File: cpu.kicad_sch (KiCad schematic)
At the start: 33 parts, among them IC12 DS2401+, IC13 ARM250, IC20 74HC138, IC27 74AC32, IC8 74HCT14, X4 72.0MHz, X5 25.175MHz

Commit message: yet more traces
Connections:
- net at C84.1, IC13.7 (~{Por}), R94.2: now also D19.1 (A); no longer D19.2 (A)
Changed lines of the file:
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@@
 		(lib_id "Device:D_Dual_CommonCathode_AAK")
 		(at 106.68 62.23 90)
-		(mirror x)
 		(unit 1)
 		(exclude_from_sim no)

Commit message: keyboard routing
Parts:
- added R83, R84, R85, R86, R87, R88, R91: 4K7, Resistor_SMD:R_0805_2012Metric, symbol Device:R_Small
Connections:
- net +5V: now also R83.2, R84.2, R85.2, R86.2, R87.2, R88.2, R91.1
- net ~{Fintr}: now also R85.1
- net ~{Pfiq}: now also R84.1
- net ~{Pirq}: now also R83.1
- net ~{Sintr}: now also R86.1
- net ~{EFiq}: now reaches IC13.134 (Efiq)
- net ~{EFiq}: now also R87.1
- net at IC13.138 (C2): now also R88.1
- net at IC13.143 (~{I13}): now also R91.2
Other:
- moved on the sheet: R218

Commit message: more analogue video work
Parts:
- added CX1: 47pF, Capacitor_THT:C_Axial_L5.1mm_D3.1mm_P12.50mm_Horizontal, symbol Device:C_Small
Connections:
- net ~{Rst}: now also CX1.2
- net at C98.2, C99.2: now also CX1.1
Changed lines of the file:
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@@
 	)
 	(junction
+		(at 71.12 88.9)
+		(diameter 0)
+		(color 0 0 0 0)
+	)
+	(junction
 		(at 187.96 86.36)
 		(diameter 0)
@@
 	(wire
 		(pts
-			(xy 63.5 88.9) (xy 78.74 88.9)
+			(xy 63.5 88.9) (xy 71.12 88.9)
 		)
 		(stroke
@@
 	(wire
 		(pts
+			(xy 71.12 88.9) (xy 71.12 90.17)
+		)
+		(stroke
+			(width 0)
+			(type default)
+		)
+	)
+	(wire
+		(pts
 			(xy 68.58 137.16) (xy 73.66 137.16)
 		)
@@
 		)
 	)
+	(wire
+		(pts
+			(xy 71.12 96.52) (xy 71.12 95.25)
+		)
+		(stroke
+			(width 0)
+			(type default)
+		)
+	)
 	(bus
 		(pts
@@
 	(wire
 		(pts
+			(xy 71.12 88.9) (xy 78.74 88.9)
+		)
+		(stroke
+			(width 0)
+			(type default)
+		)
+	)
+	(wire
+		(pts
 			(xy 186.69 232.41) (xy 189.23 232.41)
 		)
@@
 		)
 	)
+	(global_label "~{Rst}"
+		(shape input)
+		(at 71.12 96.52 0)
+		(fields_autoplaced yes)
+		(effects
+			(font
+				(size 1.27 1.27)
+			)
+			(justify left)
+		)
+		(property "Intersheetrefs" "${INTERSHEET_REFS}"
+			(at 77.129 96.52 0)
+			(effects
+				(font
+					(size 1.27 1.27)
+				)
+				(justify left)
+				(hide yes)
+			)
+		)
+	)
 	(global_label "SndVSS"
 		(shape passive)
@@
 				)
 			)
+		)
+	)
+	(symbol
+		(lib_id "Device:C_Small")
+		(at 71.12 92.71 0)
+		(mirror y)
+		(unit 1)
+		(exclude_from_sim no)
+		(in_bom yes)
+		(on_board yes)
+		(dnp no)
+		(property "Reference" "CX1"
+			(at 73.66 93.9865 0)
+			(effects
+				(font
+					(size 1.27 1.27)
+				)
+				(justify right)
+			)
+		)
+		(property "Value" "47pF"
+			(at 73.66 91.4465 0)
+			(effects
+				(font
+					(size 1.27 1.27)
+				)
+				(justify right)
+			)
+		)
+		(property "Footprint" "Capacitor_THT:C_Axial_L5.1mm_D3.1mm_P12.50mm_Horizontal"
+			(at 71.12 92.71 0)
+			(effects
+				(font
+					(size 1.27 1.27)
+				)
+				(hide yes)
+			)
+		)
+		(property "Datasheet" "~"
+			(at 71.12 92.71 0)
+			(effects
+				(font
+					(size 1.27 1.27)
+				)
+				(hide yes)
+			)
+		)
+		(property "Description" "Unpolarized capacitor, small symbol"
+			(at 71.12 92.71 0)
+			(effects
+				(font
+					(size 1.27 1.27)
+				)
+				(hide yes)
+			)
+		)
+		(pin "1"
+		)
+		(pin "2"
+		)
+		(instances
+			(project "Acorn-A3010"
+				(path "/999882f3-94f8-4a89-9093-27a47d0cb289/5f74aac3-9761-4bed-8486-119acb837e61"
+					(reference "CX1")
+					(unit 1)
+				)
+			)

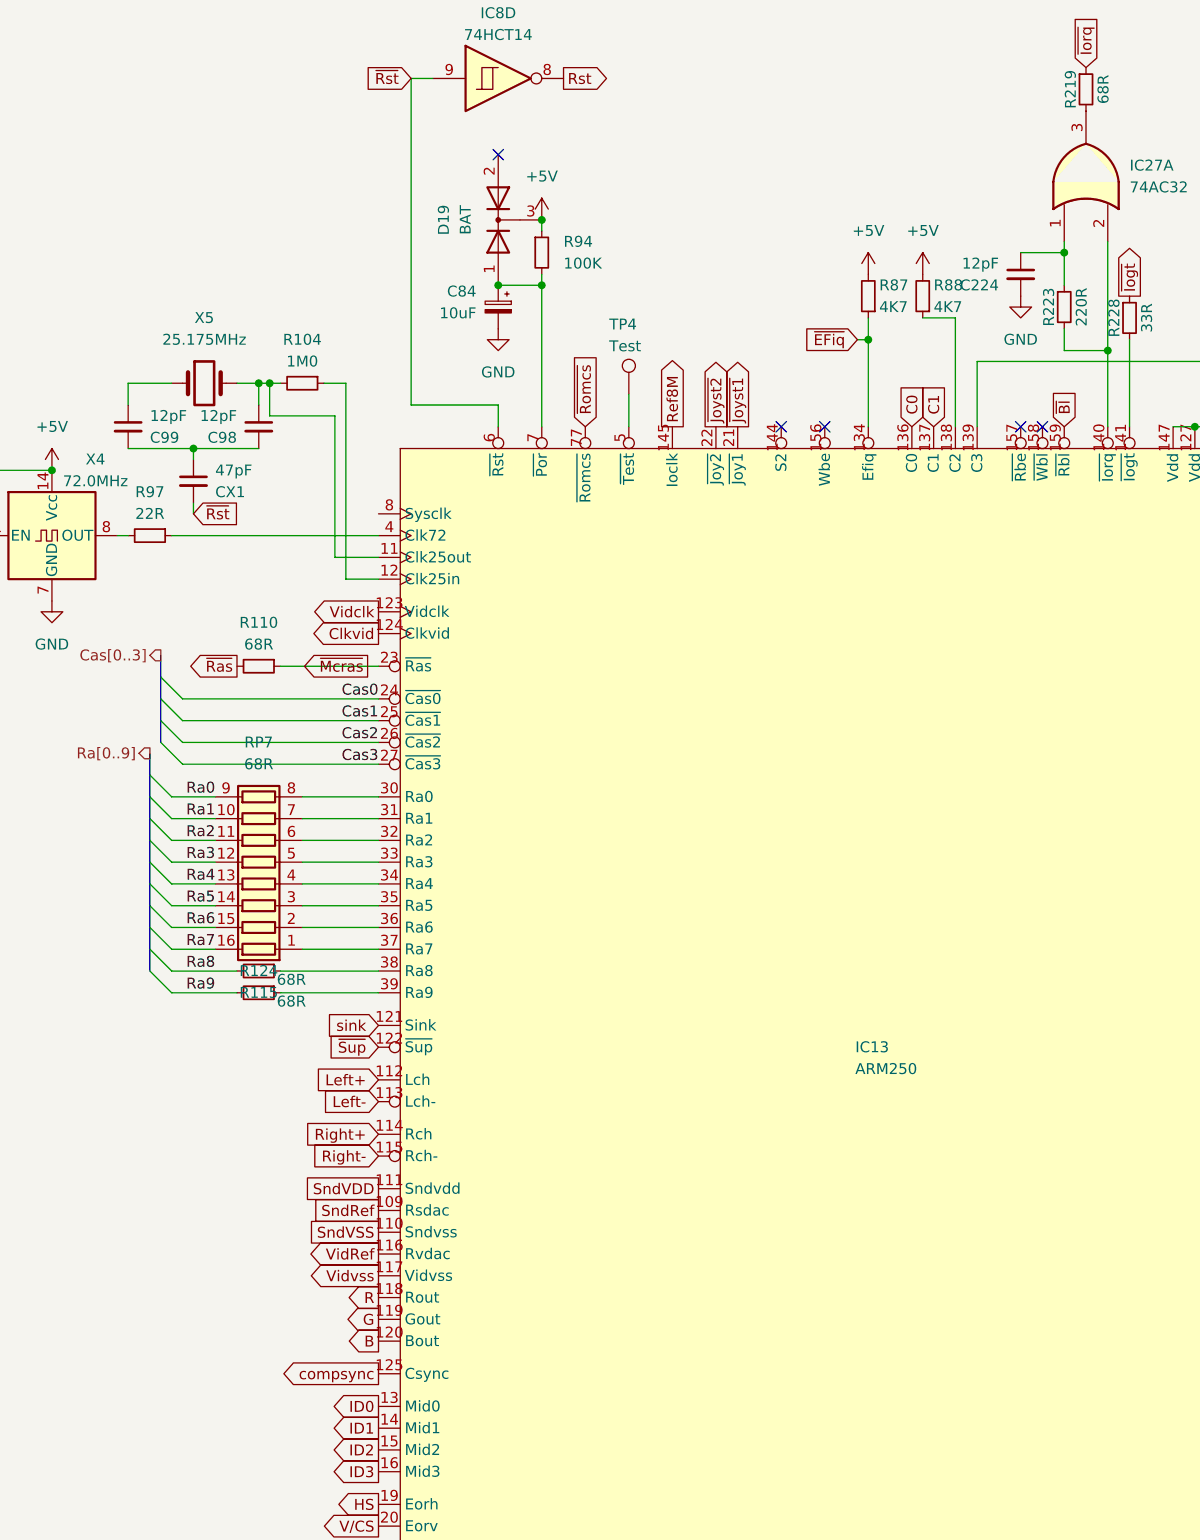
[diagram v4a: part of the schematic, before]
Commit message: adjust shielding perimeter trace and mounting holes
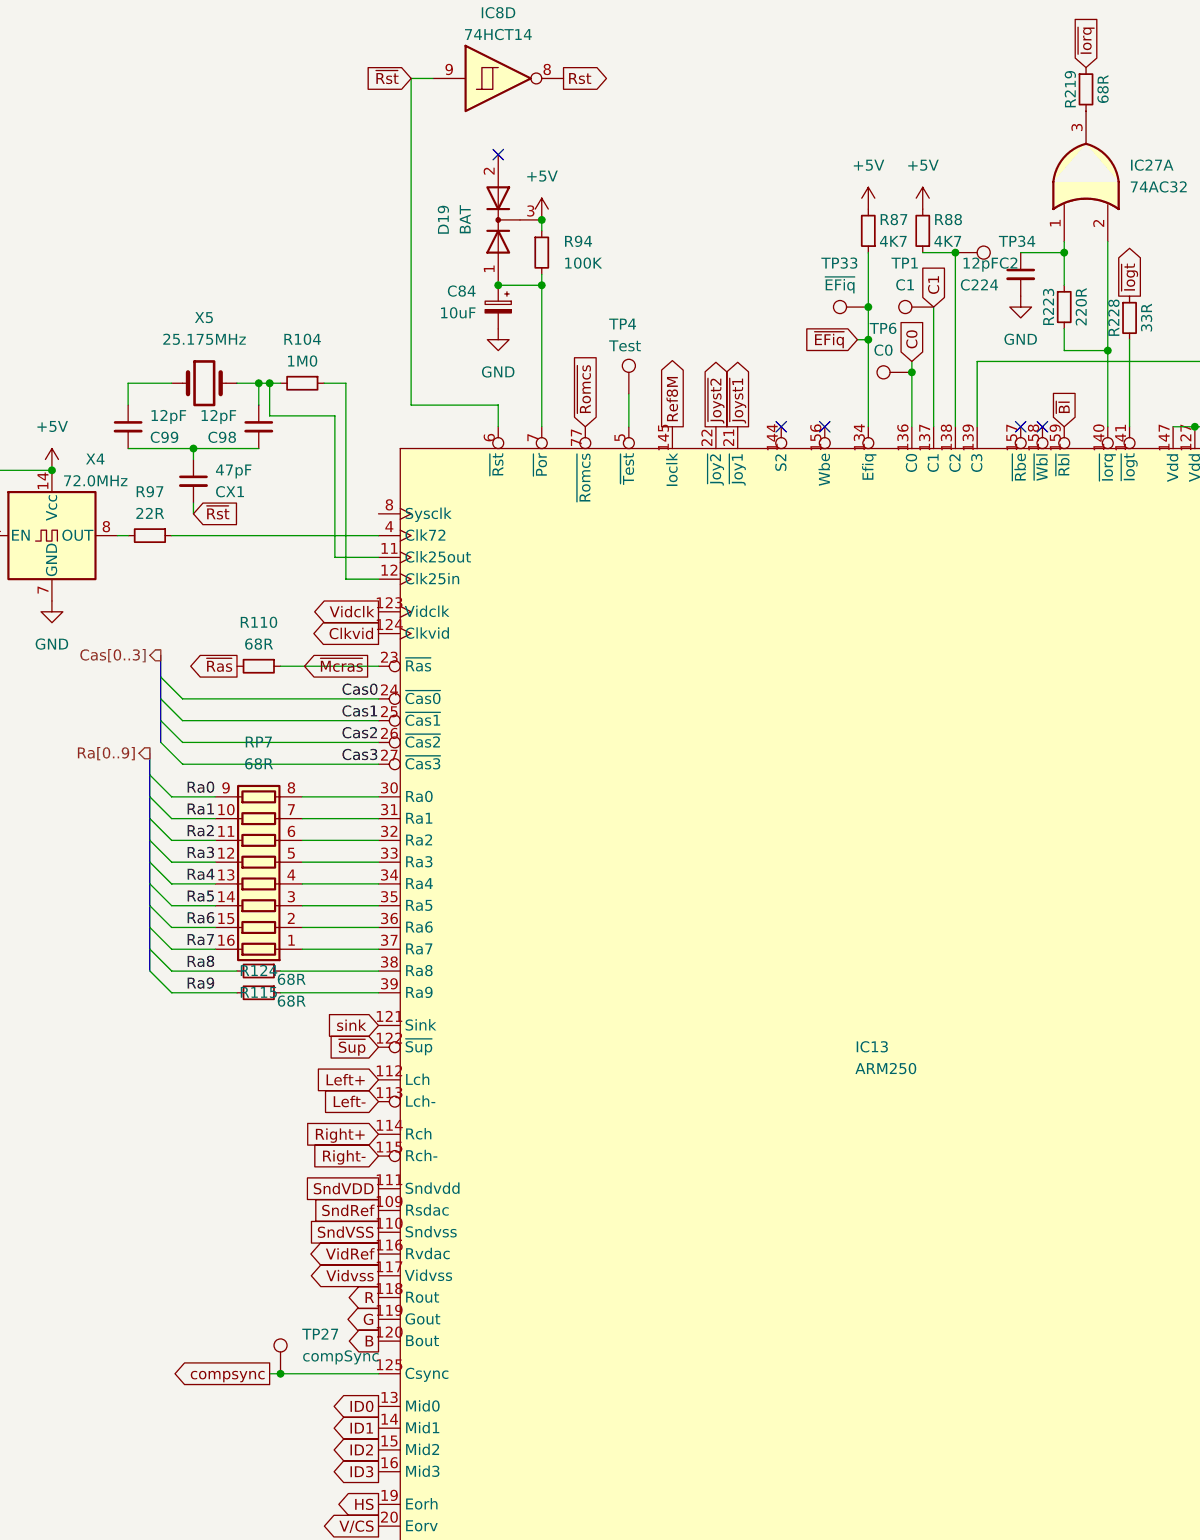
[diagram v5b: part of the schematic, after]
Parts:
- added TP1: C1, TestPoint:TestPoint_Pad_D1.0mm, symbol Connector:TestPoint
- added TP27: compSync, TestPoint:TestPoint_Pad_D1.0mm, symbol Connector:TestPoint
- added TP33: ~{EFiq}, TestPoint:TestPoint_Pad_D1.0mm, symbol Connector:TestPoint
- added TP34: C2, TestPoint:TestPoint_Pad_D1.0mm, symbol Connector:TestPoint
- added TP6: C0, TestPoint:TestPoint_Pad_D1.0mm, symbol Connector:TestPoint
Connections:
- net C0: now also TP6.1
- net C1: now also TP1.1
- net compsync: now also TP27.1
- net ~{EFiq}: now also TP33.1
- net at IC13.138 (C2), R88.1: now also TP34.1
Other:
- moved on the sheet: R87, R88

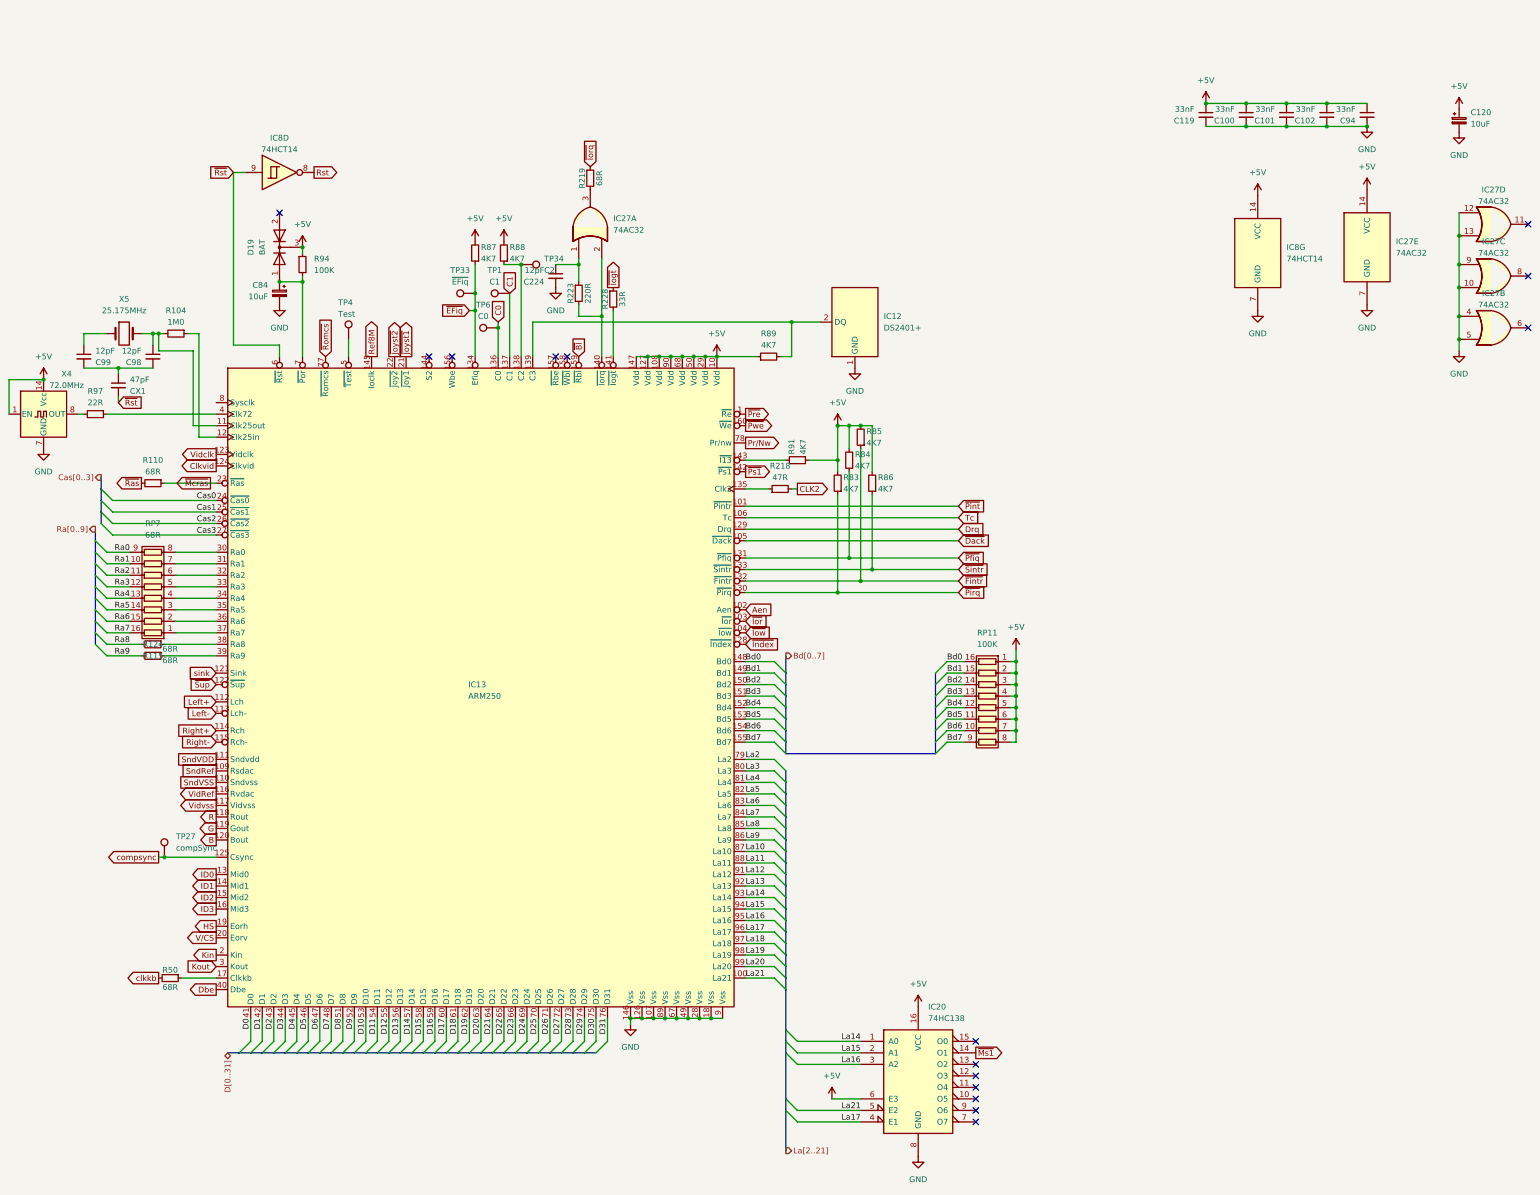
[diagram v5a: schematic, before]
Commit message: add ide and rework onboard ram
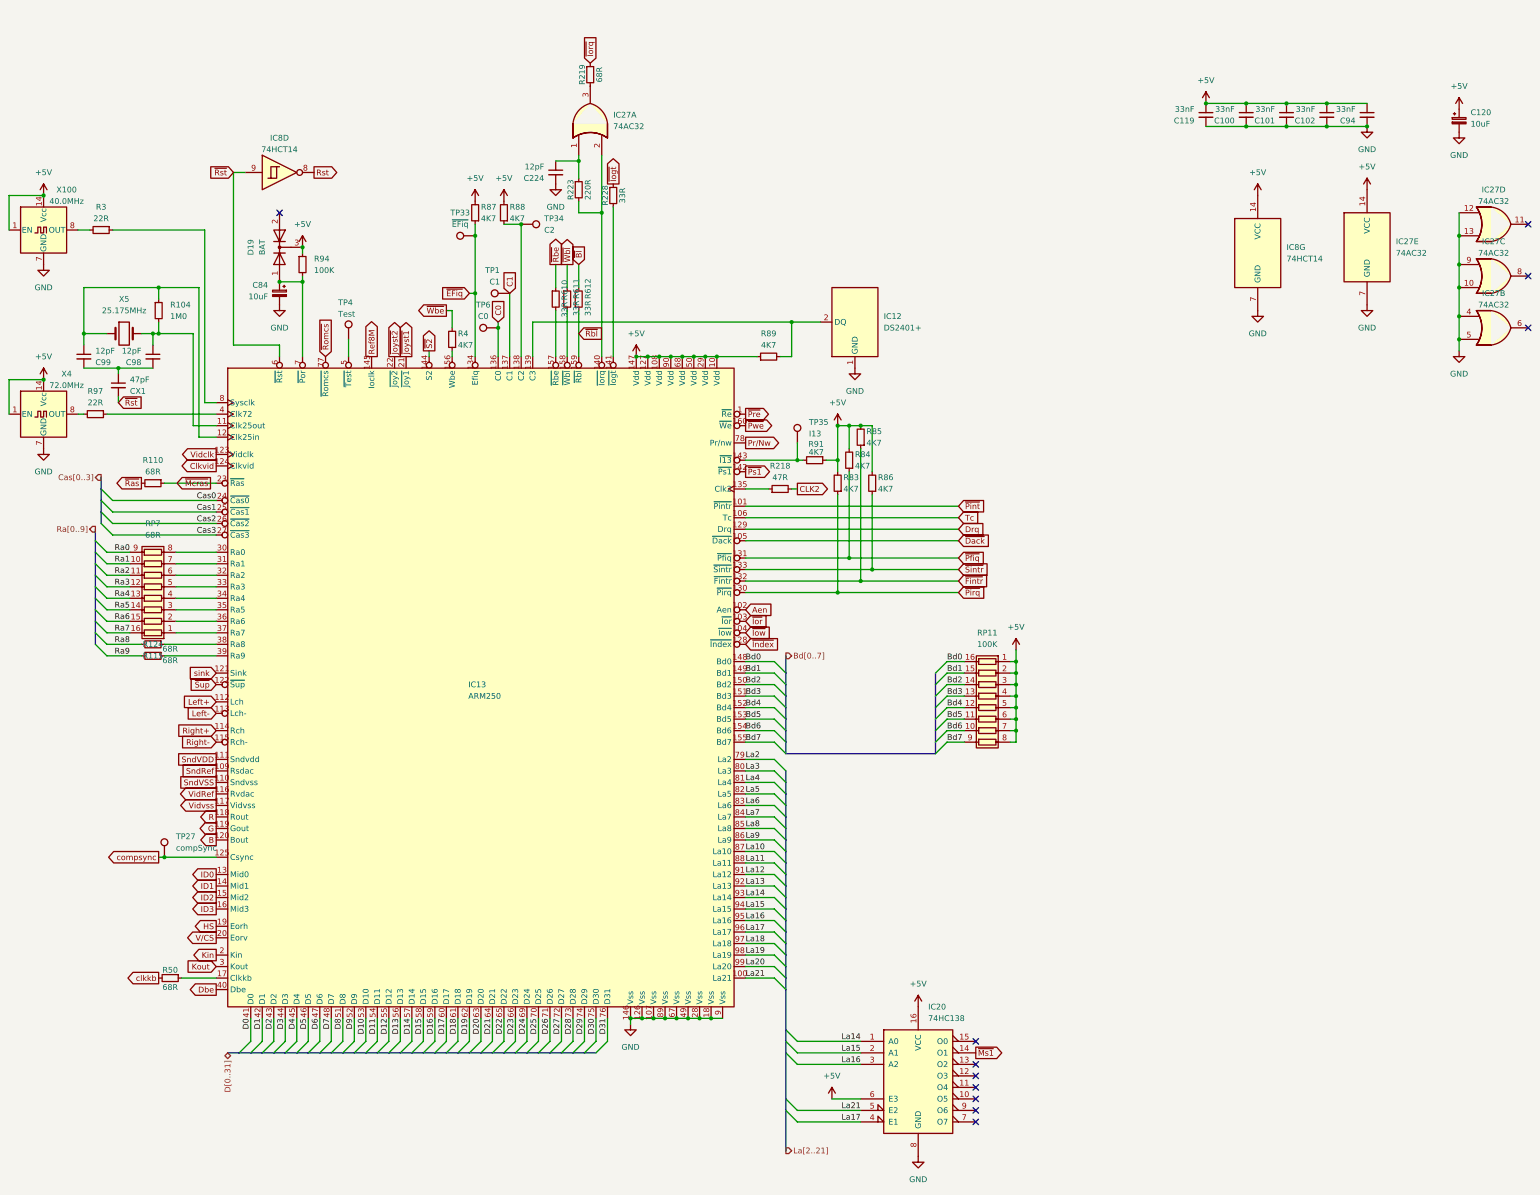
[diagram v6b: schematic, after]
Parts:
- added R3: 22R, Resistor_SMD:R_0805_2012Metric, symbol Device:R_Small
- added R4: 4K7, Resistor_SMD:R_0805_2012Metric, symbol Device:R_Small
- added R610, R611, R612: 33R, Resistor_SMD:R_0805_2012Metric, symbol Device:R_Small
- added TP35: I13, TestPoint:TestPoint_Pad_D1.0mm, symbol Connector:TestPoint
- added X100: 40.0MHz, Oscillator:Oscillator_DIP-14, symbol Oscillator:CXO_DIP14
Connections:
- net +5V: now also X100.1 (EN), X100.14 (Vcc)
- net GND: now also X100.7 (GND)
- net ~{Bl}: now also R612.1; no longer IC13.159 (~{Rbl})
- net at C99.1, X5.1: now also IC13.12 (Clk25in), R104.1
- net at IC13.143 (~{I13}), R91.2: now also TP35.1
- net ~{S2}: now reaches IC13.144 (S2)
- net at IC13.156 (Wbe): now also R4.1
- net at IC13.157 (~{Rbe}): now also R610.2
- net at IC13.158 (~{Wbl}): now also R611.2
- net at IC13.8 (Sysclk): now also R3.1
- new net: R3.2, X100.8 (OUT)
- new net ~{Rbe}: R610.1
- new net ~{Rbl}: IC13.159 (~{Rbl}), R612.2
- new net ~{Wbe}: R4.2
- new net ~{Wbl}: R611.1
- no-connect marks 15 -> 11
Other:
- moved on the sheet: C224, IC27A, R104, R219, R223, R228, R87, R88, R91, TP33, TP34
